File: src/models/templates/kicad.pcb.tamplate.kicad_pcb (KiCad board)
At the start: 2 copper layers, 0 parts

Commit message: works without arrays
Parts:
- added D1: D_Small, Keebio-Parts:Diode-dual, F.Cu at (30.8, 40.5)
- added MX1: MX-NoLED, Keebio-Parts:MX_PCB_100H, F.Cu at (43.1, 39.1)
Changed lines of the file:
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@@
     (tracks 0)
     (zones 0)
-    (modules 0)
-    (nets 1)
+    (modules 2)
+    (nets 5)
   )
   (page A4)
@@
     (solder_mask_min_width 0.25)
     (aux_axis_origin 0 0)
-    (visible_elements FFFFEF7F)
+    (visible_elements 7FFFEFFF)
     (pcbplotparams
       (layerselection 0x010fc_ffffffff)
@@
   )
   (net 0 "")
+  (net 1 "Net-(D1-Pad1)")
+  (net 2 "Net-(D1-Pad2)")
+  (net 3 "Net-(MX1-Pad2)")
+  (net 4 "Net-(MX1-Pad1)")
   (net_class Default "This is the default net class."
     (clearance 0.2)
@@
     (uvia_dia 0.3)
     (uvia_drill 0.1)
+    (add_net "Net-(D1-Pad1)")
+    (add_net "Net-(D1-Pad2)")
+    (add_net "Net-(MX1-Pad1)")
+    (add_net "Net-(MX1-Pad2)")
+  )
+  (module Keebio-Parts:MX_PCB_100H (layer F.Cu)
+    (at 43.144201 39.0872)
+    (fp_text reference MX1 (at 0 3.175) (layer F.SilkS)
+      (effects (font (size 1.27 1.524) (thickness 0.2032)))
+    )
+    (fp_text value MX-NoLED (at 0 5.08) (layer F.SilkS) hide
+      (effects (font (size 1.27 1.524) (thickness 0.2032)))
+    )
+    (fp_line (start -6.985 6.985) (end -6.985 -6.985) (layer Eco2.User) (width 0.1524))
+    (fp_line (start 6.985 6.985) (end -6.985 6.985) (layer Eco2.User) (width 0.1524))
+    (fp_line (start 6.985 -6.985) (end 6.985 6.985) (layer Eco2.User) (width 0.1524))
+    (fp_line (start -6.985 -6.985) (end 6.985 -6.985) (layer Eco2.User) (width 0.1524))
+    (fp_line (start -6.35 -4.572) (end -6.35 -6.35) (layer F.SilkS) (width 0.381))
+    (fp_line (start -6.35 6.35) (end -6.35 4.572) (layer F.SilkS) (width 0.381))
+    (fp_line (start -4.572 6.35) (end -6.35 6.35) (layer F.SilkS) (width 0.381))
+    (fp_line (start 6.35 6.35) (end 4.572 6.35) (layer F.SilkS) (width 0.381))
+    (fp_line (start 6.35 4.572) (end 6.35 6.35) (layer F.SilkS) (width 0.381))
+    (fp_line (start 6.35 -6.35) (end 6.35 -4.572) (layer F.SilkS) (width 0.381))
+    (fp_line (start 4.572 -6.35) (end 6.35 -6.35) (layer F.SilkS) (width 0.381))
+    (fp_line (start -6.35 -6.35) (end -4.572 -6.35) (layer F.SilkS) (width 0.381))
+    (fp_line (start -9.398 9.398) (end -9.398 -9.398) (layer Dwgs.User) (width 0.1524))
+    (fp_line (start 9.398 9.398) (end -9.398 9.398) (layer Dwgs.User) (width 0.1524))
+    (fp_line (start 9.398 -9.398) (end 9.398 9.398) (layer Dwgs.User) (width 0.1524))
+    (fp_line (start -9.398 -9.398) (end 9.398 -9.398) (layer Dwgs.User) (width 0.1524))
+    (fp_line (start -6.35 6.35) (end -6.35 -6.35) (layer Cmts.User) (width 0.1524))
+    (fp_line (start 6.35 6.35) (end -6.35 6.35) (layer Cmts.User) (width 0.1524))
+    (fp_line (start 6.35 -6.35) (end 6.35 6.35) (layer Cmts.User) (width 0.1524))
+    (fp_line (start -6.35 -6.35) (end 6.35 -6.35) (layer Cmts.User) (width 0.1524))
+    (fp_text user 1.00u (at -5.715 8.255) (layer Dwgs.User)
+      (effects (font (size 1.524 1.524) (thickness 0.3048)))
+    )
+    (pad HOLE np_thru_hole circle (at 5.08 0) (size 1.8 1.8) (drill 1.8) (layers *.Cu))
+    (pad HOLE np_thru_hole circle (at -5.08 0) (size 1.8 1.8) (drill 1.8) (layers *.Cu))
+    (pad HOLE np_thru_hole circle (at 0 0) (size 3.9878 3.9878) (drill 3.9878) (layers *.Cu))
+    (pad 2 thru_hole circle (at -3.81 -2.54) (size 2.286 2.286) (drill 1.4986) (layers *.Cu *.SilkS *.Mask)
+      (net 3 "Net-(MX1-Pad2)"))
+    (pad 1 thru_hole circle (at 2.54 -5.08) (size 2.286 2.286) (drill 1.4986) (layers *.Cu *.SilkS *.Mask)
+      (net 4 "Net-(MX1-Pad1)"))
+  )
+  (module Keebio-Parts:Diode-dual (layer F.Cu)
+    (at 30.77 40.48 270)
+    (attr smd)
+    (fp_text reference D1 (at -0.0254 1.4) (layer F.SilkS)
+      (effects (font (size 0.8 0.8) (thickness 0.15)))
+    )
+    (fp_text value D_Small (at 0 -1.925 270) (layer F.SilkS) hide
+      (effects (font (size 0.8 0.8) (thickness 0.15)))
+    )
+    (fp_line (start -2.54 0.762) (end 2.54 0.762) (layer F.SilkS) (width 0.15))
+    (fp_line (start 2.54 0.762) (end 2.54 -0.762) (layer F.SilkS) (width 0.15))
+    (fp_line (start 2.54 -0.762) (end -2.54 -0.762) (layer F.SilkS) (width 0.15))
+    (fp_line (start -2.54 -0.762) (end -2.54 0.762) (layer F.SilkS) (width 0.15))
+    (fp_line (start -2.54 0.762) (end -2.032 0.762) (layer F.SilkS) (width 0.15))
+    (fp_line (start 2.159 0.762) (end 2.159 -0.762) (layer F.SilkS) (width 0.15))
+    (fp_line (start 2.286 -0.762) (end 2.286 0.762) (layer F.SilkS) (width 0.15))
+    (fp_line (start 2.413 0.762) (end 2.413 -0.762) (layer F.SilkS) (width 0.15))
+    (fp_line (start 2.032 -0.762) (end 2.032 0.762) (layer F.SilkS) (width 0.15))
+    (fp_line (start 1.905 0.762) (end 1.905 -0.762) (layer F.SilkS) (width 0.15))
+    (fp_line (start 1.778 0.762) (end 1.778 -0.762) (layer F.SilkS) (width 0.15))
+    (pad 1 smd rect (at 2.5 0 270) (size 2.9 0.5) (layers F.Cu)
+      (net 1 "Net-(D1-Pad1)"))
+    (pad 2 smd rect (at -2.5 0 270) (size 2.9 0.5) (layers F.Cu)
+      (net 2 "Net-(D1-Pad2)"))
+    (pad 1 thru_hole rect (at 3.9 0 270) (size 1.6 1.6) (drill 1) (layers *.Cu *.Mask F.SilkS)
+      (net 1 "Net-(D1-Pad1)"))
+    (pad 2 thru_hole circle (at -3.9 0 270) (size 1.6 1.6) (drill 1) (layers *.Cu *.Mask F.SilkS)
+      (net 2 "Net-(D1-Pad2)"))
+    (pad 2 smd rect (at -1.4 0 270) (size 1.6 1.2) (layers F.Cu F.Paste F.Mask)
+      (net 2 "Net-(D1-Pad2)"))
+    (pad 1 smd rect (at 1.4 0 270) (size 1.6 1.2) (layers F.Cu F.Paste F.Mask)
+      (net 1 "Net-(D1-Pad1)"))
+    (pad 1 smd rect (at 2.5 0 270) (size 2.9 0.5) (layers B.Cu)
+      (net 1 "Net-(D1-Pad1)"))
+    (pad 1 smd rect (at 1.4 0 270) (size 1.6 1.2) (layers B.Cu B.Paste B.Mask)
+      (net 1 "Net-(D1-Pad1)"))
+    (pad 2 smd rect (at -1.4 0 270) (size 1.6 1.2) (layers B.Cu B.Paste B.Mask)
+      (net 2 "Net-(D1-Pad2)"))
+    (pad 2 smd rect (at -2.5 0 270) (size 2.9 0.5) (layers B.Cu)
+      (net 2 "Net-(D1-Pad2)"))
+    (model ${KISYS3DMOD}/Diodes_SMD.3dshapes/D_SOD-123.step
+      (at (xyz 0 0 0))
+      (scale (xyz 1 1 1))
+      (rotate (xyz 0 0 0))
+    )
   )
 )

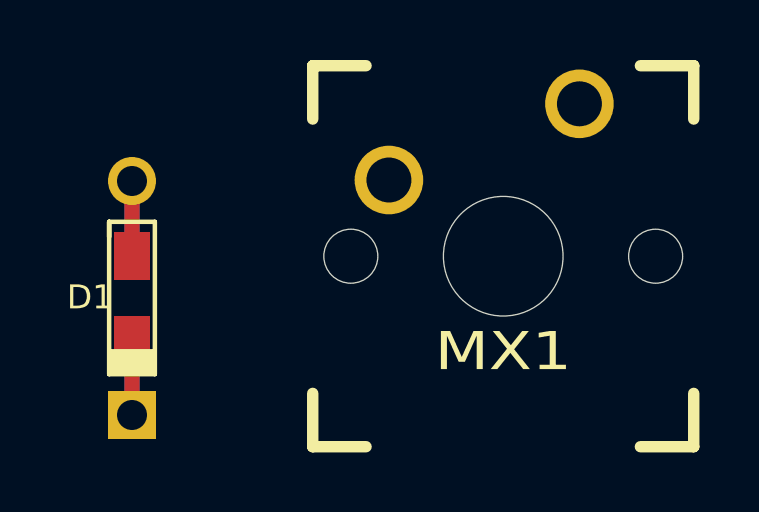
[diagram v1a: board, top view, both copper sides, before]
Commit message: make tests pass on ci by skipping
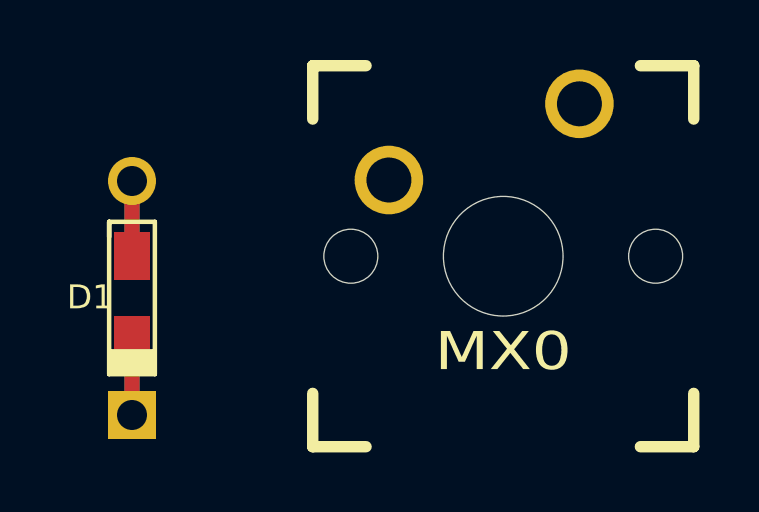
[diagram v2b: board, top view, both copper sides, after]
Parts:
- renumbered MX1 to MX0
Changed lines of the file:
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@@
   (net 1 "Net-(D1-Pad1)")
   (net 2 "Net-(D1-Pad2)")
-  (net 3 "Net-(MX1-Pad2)")
-  (net 4 "Net-(MX1-Pad1)")
+  (net 3 "Net-(MX0-Pad2)")
+  (net 4 "Net-(MX0-Pad1)")
   (net_class Default "This is the default net class."
     (clearance 0.2)
@@
     (add_net "Net-(D1-Pad1)")
     (add_net "Net-(D1-Pad2)")
-    (add_net "Net-(MX1-Pad1)")
-    (add_net "Net-(MX1-Pad2)")
+    (add_net "Net-(MX0-Pad1)")
+    (add_net "Net-(MX0-Pad2)")
   )
   (module Keebio-Parts:MX_PCB_100H (layer F.Cu)
     (at 43.144201 39.0872)
-    (fp_text reference MX1 (at 0 3.175) (layer F.SilkS)
+    (fp_text reference MX0 (at 0 3.175) (layer F.SilkS)
       (effects (font (size 1.27 1.524) (thickness 0.2032)))
     )
@@
     (pad HOLE np_thru_hole circle (at 0 0) (size 3.9878 3.9878) (drill 3.9878) (layers *.Cu))
     (pad 2 thru_hole circle (at -3.81 -2.54) (size 2.286 2.286) (drill 1.4986) (layers *.Cu *.SilkS *.Mask)
-      (net 3 "Net-(MX1-Pad2)"))
+      (net 3 "Net-(MX0-Pad2)"))
     (pad 1 thru_hole circle (at 2.54 -5.08) (size 2.286 2.286) (drill 1.4986) (layers *.Cu *.SilkS *.Mask)
-      (net 4 "Net-(MX1-Pad1)"))
+      (net 4 "Net-(MX0-Pad1)"))
   )
   (module Keebio-Parts:Diode-dual (layer F.Cu)
